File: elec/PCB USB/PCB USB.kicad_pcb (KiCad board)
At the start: 2 copper layers, 75 x 25 mm, 93 parts, among them J201 USB_C_PICO, J402 USB_C_Receptacle_USB2.0_14P, J403 USB_A, J404 USB_C_Receptacle_USB2.0_14P, J405 USB_A, J501 Conn_I2C_Écran, Q301 AO3401A, Q401 AO3401A, SW201 SW_BOOTSEL, SW202 SW_RESET, SW501 RotaryEncoder_Switch, U201 SRV05-4, U202 RP2350B-QFN80, U203 W25Q128JVPIQ, U301 AP7361C-33E, U401 SRV05-4, Y201 CM4012M00012001, Y401 12MHz

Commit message: PUSHHHHHHHHHHHH
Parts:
- added P1: USB_C_Plug_USB2.0, JT_USB_C:UP20-C-F-G-FL-1-P12-TR, F.Cu at (174.3, 97.0)
- moved J201 96.1 mm to (145.0, 108.0)
- moved SW501 85.3 mm to (105.0, 97.5)
- moved U201 2.42 mm to (72.1, 73.0)
- moved R203 0.72 mm to (66.9, 47.5)
- moved R204 0.72 mm to (66.9, 50.0)
- moved R205 0.72 mm to (66.9, 52.5)
- moved C201 0.72 mm to (54.9, 47.5)
- moved C202 0.72 mm to (54.9, 50.0)
- moved C203 0.72 mm to (54.9, 52.5)
- moved C204 0.72 mm to (54.9, 55.1)
- moved C205 0.72 mm to (54.9, 57.6)
- moved C206 0.72 mm to (54.9, 60.1)
- moved C207 0.72 mm to (58.9, 47.5)
- moved C208 0.72 mm to (58.9, 50.0)
- moved C209 0.72 mm to (58.9, 52.5)
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
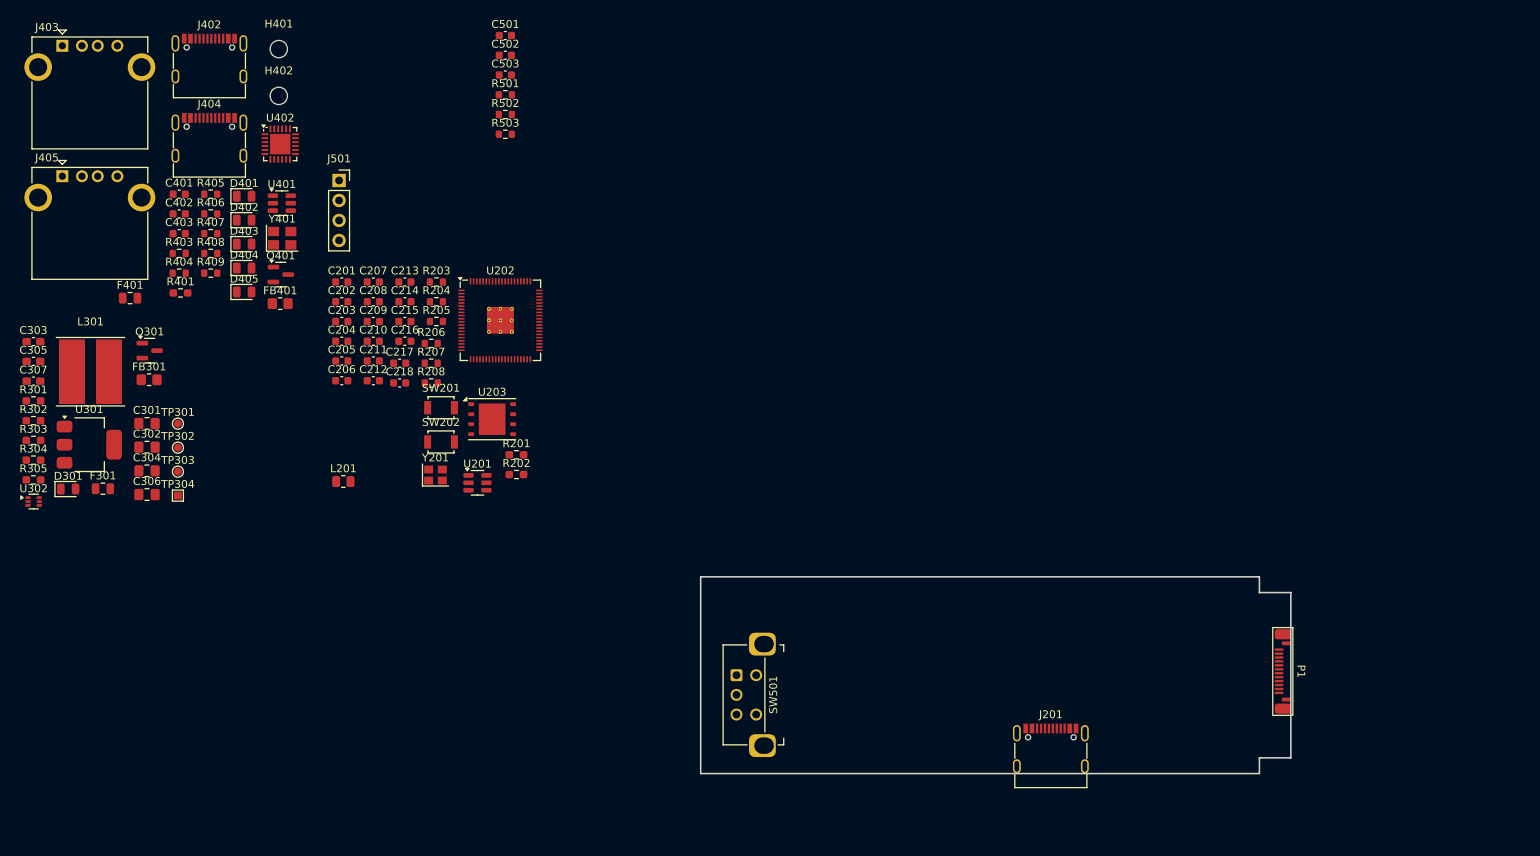
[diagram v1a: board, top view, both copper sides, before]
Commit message: placements trucs usb
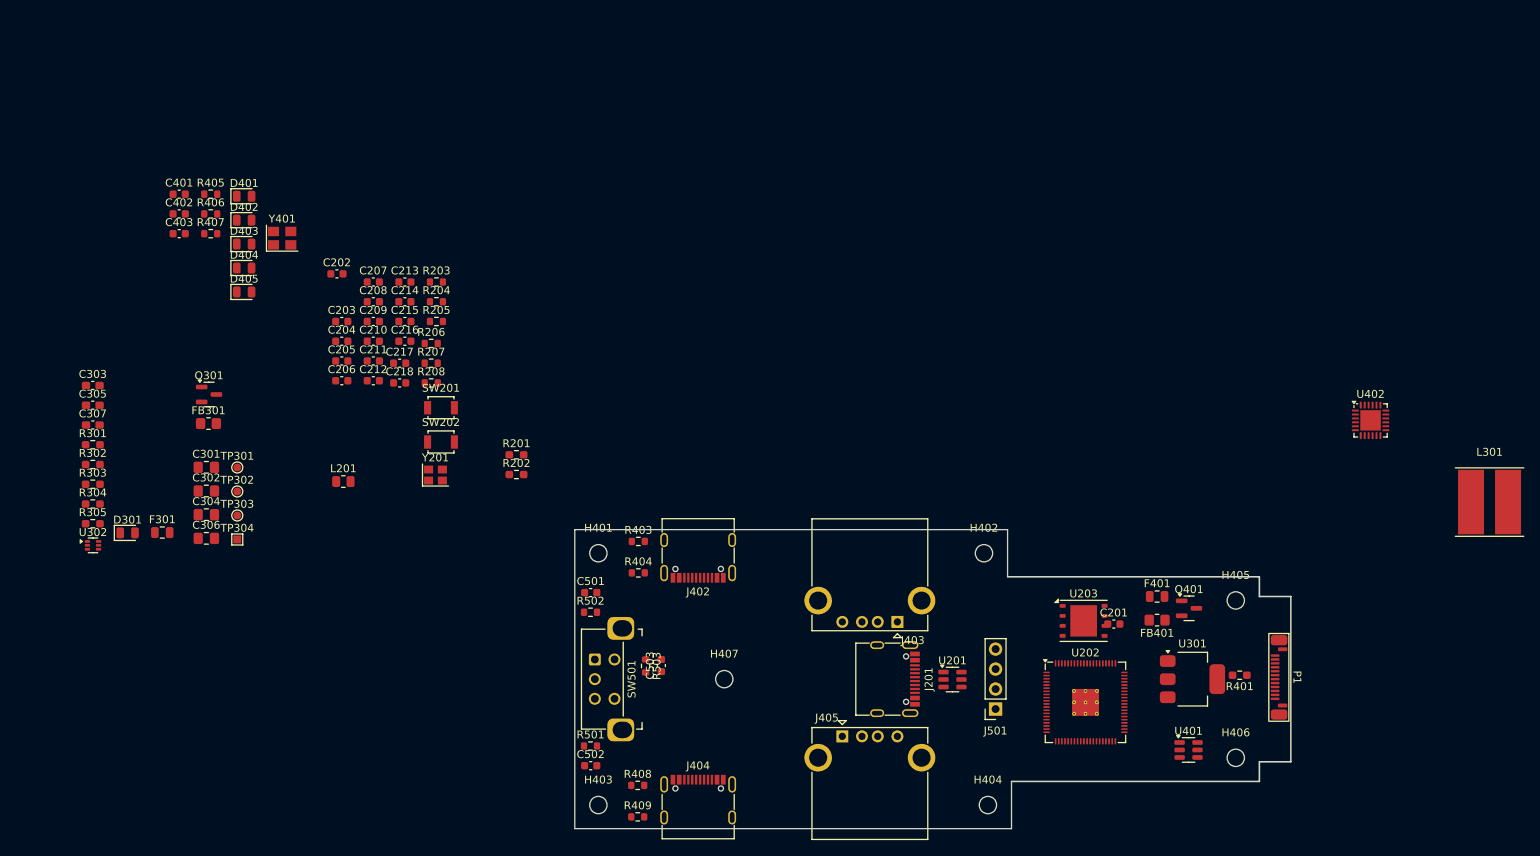
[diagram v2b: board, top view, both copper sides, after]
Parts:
- added H403: MountingHole, MountingHole:MountingHole_2.2mm_M2, F.Cu at (87.5, 114.0)
- added H404: MountingHole, MountingHole:MountingHole_2.2mm_M2, F.Cu at (137.0, 114.0)
- added H405: MountingHole, MountingHole:MountingHole_2.2mm_M2, F.Cu at (168.5, 88.0)
- added H406: MountingHole, MountingHole:MountingHole_2.2mm_M2, F.Cu at (168.5, 108.0)
- added H407: MountingHole, MountingHole:MountingHole_2.2mm_M2, F.Cu at (103.5, 98.0)
- moved L301 178.6 mm to (200.8, 75.5)
- moved U301 143.3 mm to (163.0, 98.0)
- moved R401 143.1 mm to (169.0, 97.5), turned to 180 degrees
- moved U402 142.9 mm to (185.6, 65.1)
- moved F401 135.9 mm to (158.5, 87.5)
- moved U401 134.6 mm to (162.5, 107.0)
- moved J403 128.9 mm to (125.5, 90.7), turned to 180 degrees
- moved Q401 123.0 mm to (162.6, 89.0)
- moved J405 122.0 mm to (118.5, 105.3)
- moved FB401 118.5 mm to (158.5, 90.5), turned to 180 degrees
- moved C201 107.3 mm to (153.0, 91.0)
- moved J501 107.1 mm to (138.0, 101.8), turned to 180 degrees
- moved H402 106.8 mm to (136.5, 82.0)
- moved J404 104.5 mm to (100.2, 114.5)
- moved C502 90.9 mm to (86.5, 109.0)
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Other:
- board size 75 x 25 mm -> 91 x 38 mm

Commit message: speed
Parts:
- C501, R403, R404, R502: moved to B.Cu
- moved J201 39.5 mm to (86.9, 84.4)
- moved H403 22.0 mm to (109.5, 114.0)
- moved H401 21.5 mm to (109.0, 82.0)
- moved R502 1.02 mm to (86.7, 90.5), turned to 180 degrees
- moved R404 0.10 mm to (92.7, 84.5), turned to 180 degrees
- turned C501 to 180 degrees
- turned R403 to 180 degrees

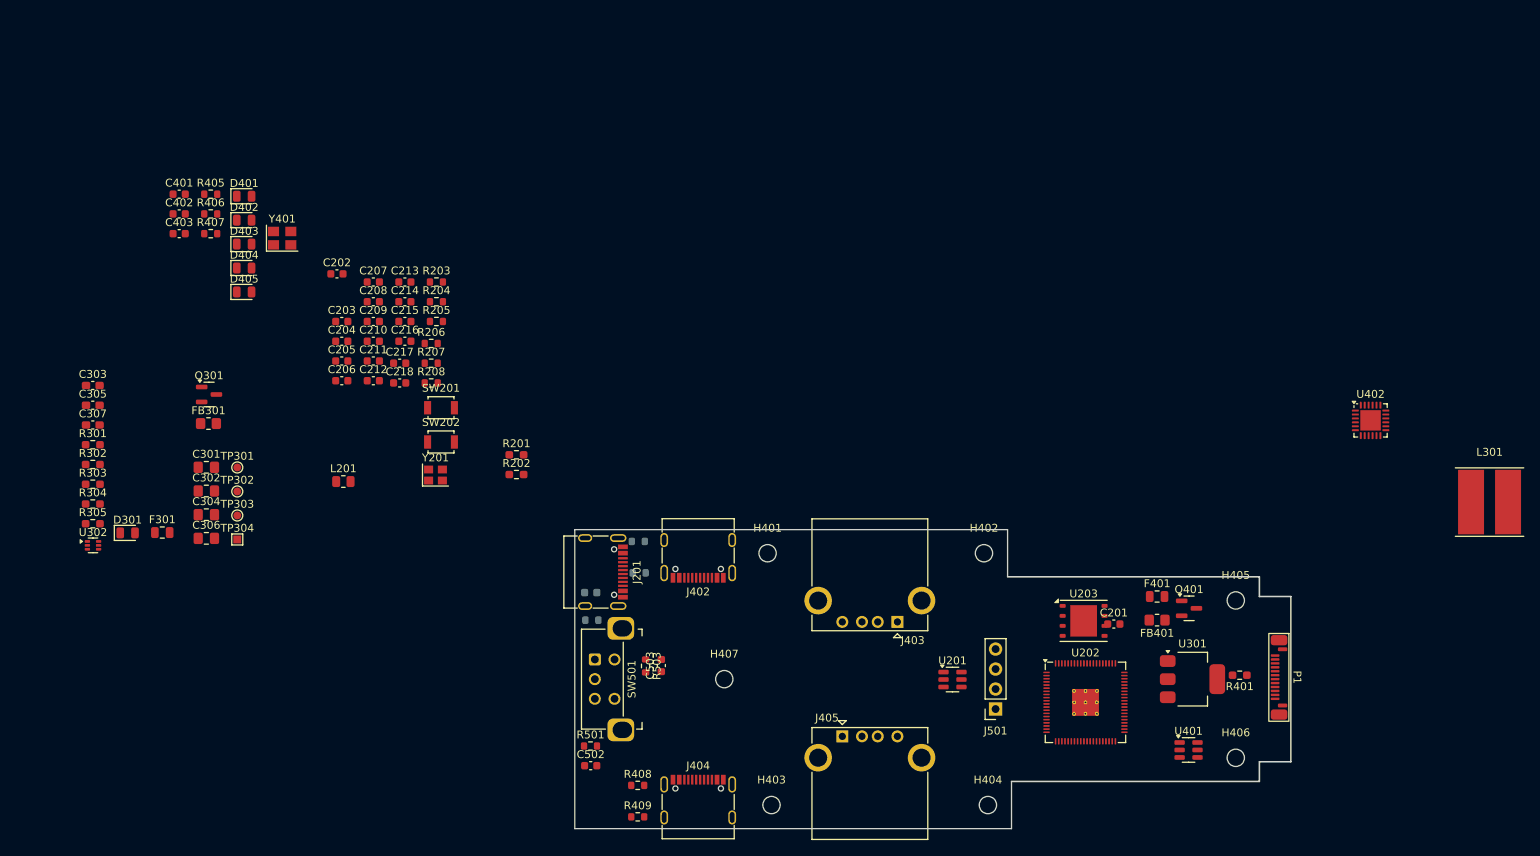
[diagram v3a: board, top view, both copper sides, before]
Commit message: All components placed (no traces yet tho)
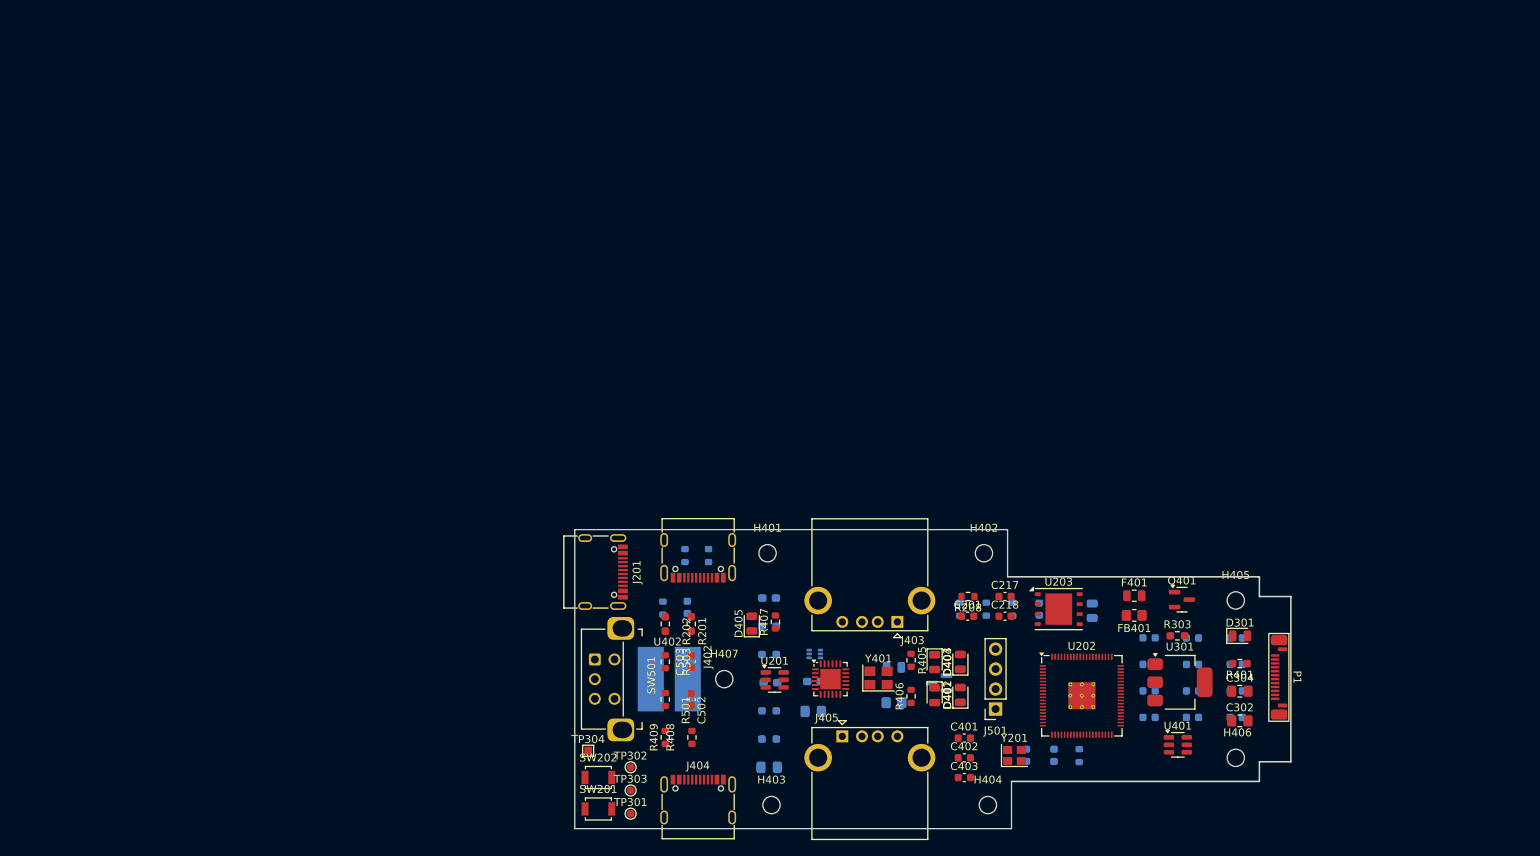
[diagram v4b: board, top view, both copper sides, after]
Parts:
- C202, C203, C204, C205, C206, C207, C208, C209, C210, C211, C212, C213, C214, C215, C216, C301, C303, C305, C306, C307, F301, FB301, L201, L301, Q301, R203, R204, R205, R206, R207, R301, R302, R304, R305, U302: moved to B.Cu
- moved D301 142.0 mm to (169.0, 92.5)
- moved R303 139.2 mm to (161.1, 92.5)
- moved C302 134.5 mm to (169.0, 103.3)
- moved C304 133.2 mm to (169.0, 99.5)
- moved C401 121.4 mm to (134.0, 105.5)
- moved C402 121.4 mm to (134.0, 108.0)
- moved C403 121.4 mm to (134.0, 110.5)
- moved C212 117.7 mm to (168.6, 102.9), turned to 180 degrees
- moved C202 117.6 mm to (157.5, 102.9), turned to 180 degrees
- moved C211 117.4 mm to (168.6, 99.5), turned to 180 degrees
- moved C210 117.1 mm to (168.6, 96.1), turned to 180 degrees
- moved C209 116.8 mm to (168.6, 92.8), turned to 180 degrees
- moved C208 116.7 mm to (163.0, 102.9), turned to 180 degrees
- moved C207 116.4 mm to (163.0, 99.5), turned to 180 degrees
- moved C206 114.0 mm to (163.0, 96.1), turned to 180 degrees
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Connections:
- D405 pad 1: unconnected-(D405-K-Pad1) -> Net-(D405-K)
- R407 pad 1: unconnected-(R407-Pad1) -> Net-(D405-K)

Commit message: push pcb
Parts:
- removed C301: 10µF, Capacitor_SMD:C_0805_2012Metric_Pad1.18x1.45mm_HandSolder
- removed C303, C307: 0.1µF, Capacitor_SMD:C_0603_1608Metric_Pad1.08x0.95mm_HandSolder
- removed C305: 33pF, Capacitor_SMD:C_0603_1608Metric_Pad1.08x0.95mm_HandSolder
- removed C306: 22µF, Capacitor_SMD:C_0805_2012Metric_Pad1.18x1.45mm_HandSolder
- removed L301: 2.2uH 13.2mOhm, Inductor_SMD:L_TDK_VLP8040
- removed R301: 100k, Resistor_SMD:R_0603_1608Metric_Pad0.98x0.95mm_HandSolder
- removed R302: 17.4k, Resistor_SMD:R_0603_1608Metric_Pad0.98x0.95mm_HandSolder
- removed R304: 220k, Resistor_SMD:R_0603_1608Metric_Pad0.98x0.95mm_HandSolder
- removed R305: 30k, Resistor_SMD:R_0603_1608Metric_Pad0.98x0.95mm_HandSolder
- removed TP303: TP_5V, TestPoint:TestPoint_Pad_D1.0mm
- removed TP304: TP_GND, TestPoint:TestPoint_Pad_1.0x1.0mm
- removed U302: ~, Package_TO_SOT_SMD:SOT-563
- C201, C217, C218, R201, R202, R208, R303, R401, R407, R408, R409: moved to B.Cu
- C209, C213, C216, C401, C402: footprint Capacitor_SMD:C_0603_1608Metric -> Capacitor_SMD:C_0805_2012Metric
- C214, C215, C501, F301, FB301, Q301, R206, R207, R502: moved to F.Cu
- moved R203 61.2 mm to (87.5, 110.5), turned to 0 degrees
- moved Q401 54.7 mm to (107.2, 93.3)
- moved R204 52.5 mm to (87.5, 114.5), turned to 0 degrees
- moved FB401 48.6 mm to (107.5, 96.9), turned to -90 degrees
- moved R207 46.4 mm to (93.8, 88.8), turned to 0 degrees
- moved F401 45.9 mm to (110.2, 94.3), turned to 90 degrees
- moved F301 45.4 mm to (170.4, 97.8), turned to 180 degrees
- moved R206 43.0 mm to (93.8, 87.3), turned to 180 degrees
- moved FB301 41.9 mm to (166.3, 93.8)
- moved D401 39.5 mm to (93.8, 115.2), turned to 90 degrees
- moved Q301 39.5 mm to (170.1, 95.0)
- moved D404 39.4 mm to (93.9, 80.7)
- moved D301 25.7 mm to (143.8, 87.3), turned to -90 degrees
- moved C209 23.5 mm to (148.0, 104.1), turned to 90 degrees
- moved D403 19.5 mm to (131.9, 115.2)
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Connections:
- FB301 pad 2: +5V_PROTECT -> +5V
- TP301 pad 1: +5V_PROTECT -> +5V
- Y401 pad 2: Net-(U402-X_{IN}) -> (no net)
- Y401 pad 3: (no net) -> Net-(U402-X_{IN})
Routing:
- net /USB_HUB/D-: track 0.00 -> 64.3 mm, vias 0 -> 2
- net /MCU/D-: track 0.00 -> 63.2 mm, vias 0 -> 2
- net /MCU/D+: track 0.00 -> 63.1 mm, vias 0 -> 2
- net /USB_HUB/D+: track 0.00 -> 61.3 mm, vias 0 -> 2
- net VBUS: track 0.00 -> 60.4 mm, vias 0 -> 9
- net /USB_HUB/USBC_1_D+: track 0.00 -> 50.4 mm
- net /USB_HUB/USBC_1_D-: track 0.00 -> 50.4 mm
- net /USB_HUB/USBC_2_D+: track 0.00 -> 34.1 mm, vias 0 -> 2
- net /USB_HUB/USBC_2_D-: track 0.00 -> 34.1 mm, vias 0 -> 2
- net +5V: track 0.00 -> 21.6 mm
- net GND: track 0.00 -> 17.5 mm
- net /USB_HUB/USBA_2_D-: track 0.00 -> 14.1 mm, vias 0 -> 1
- net /USB_HUB/USBA_2_D+: track 0.00 -> 14.1 mm, vias 0 -> 1
- net +3V3: track 0.00 -> 11.7 mm, vias 0 -> 6
- net /MCU/USB_PICO_D+: track 0.00 -> 10.8 mm
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- added copper zone on In2.Cu, net +3V3
- added copper zone on B.Cu, net GND
- added copper zone on F.Cu, net GND
- added copper zone on In1.Cu, net GND
- added copper zone on In2.Cu, net VBUS
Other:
- copper layers 2 -> 4

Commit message: oh shit game de volley
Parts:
- moved R406 2.20 mm to (121.0, 93.9)
- moved R405 1.20 mm to (122.9, 93.8)
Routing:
- net VBUS: track 60.4 -> 248.9 mm, vias 9 -> 11
- net Net-(D401-A): track 0.00 -> 152.9 mm, vias 0 -> 2
- net +3V3: track 11.7 -> 113.6 mm, vias 6 -> 10
- net /MCU/~{QSPI_CS_{0}}: track 0.00 -> 101.1 mm
- net Net-(D401-K): track 0.00 -> 79.4 mm, vias 0 -> 3
- net Net-(D403-K): track 0.00 -> 76.8 mm, vias 0 -> 3
- net /MCU/~{RESET}: track 2.38 -> 71.1 mm, vias 1 -> 6
- net /MCU/GPIO6: track 1.62 -> 64.3 mm, vias 0 -> 2
- net /MCU/GPIO7: track 1.51 -> 63.8 mm, vias 0 -> 2
- net /MCU/GPIO8: track 1.52 -> 63.7 mm
- net /MCU/USB_PICO_D+: track 10.8 -> 36.0 mm
- net /MCU/USB_PICO_D-: track 10.6 -> 34.1 mm
- net /MCU/QSPI_SD3: track 0.00 -> 11.1 mm
- net /MCU/QSPI_SCLK: track 0.00 -> 9.53 mm
- net Net-(U202-XIN): track 0.00 -> 8.98 mm, vias 0 -> 2
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- removed copper zone on B.Cu, net GND
- removed copper zone on F.Cu, net GND
- removed copper zone on In1.Cu, net GND
